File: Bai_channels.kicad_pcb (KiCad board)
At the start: 2 copper layers, 119 parts, among them Q1 BC337, Q10 BC337, Q11 BC337, Q12 BC337, Q2 BC337, Q3 BC337, Q4 BC337, Q5 BC337, Q6 BC337, Q7 BC337, Q8 BC337, Q9 BC337, U2 ATmega328-P, U3 LM7805_TO220

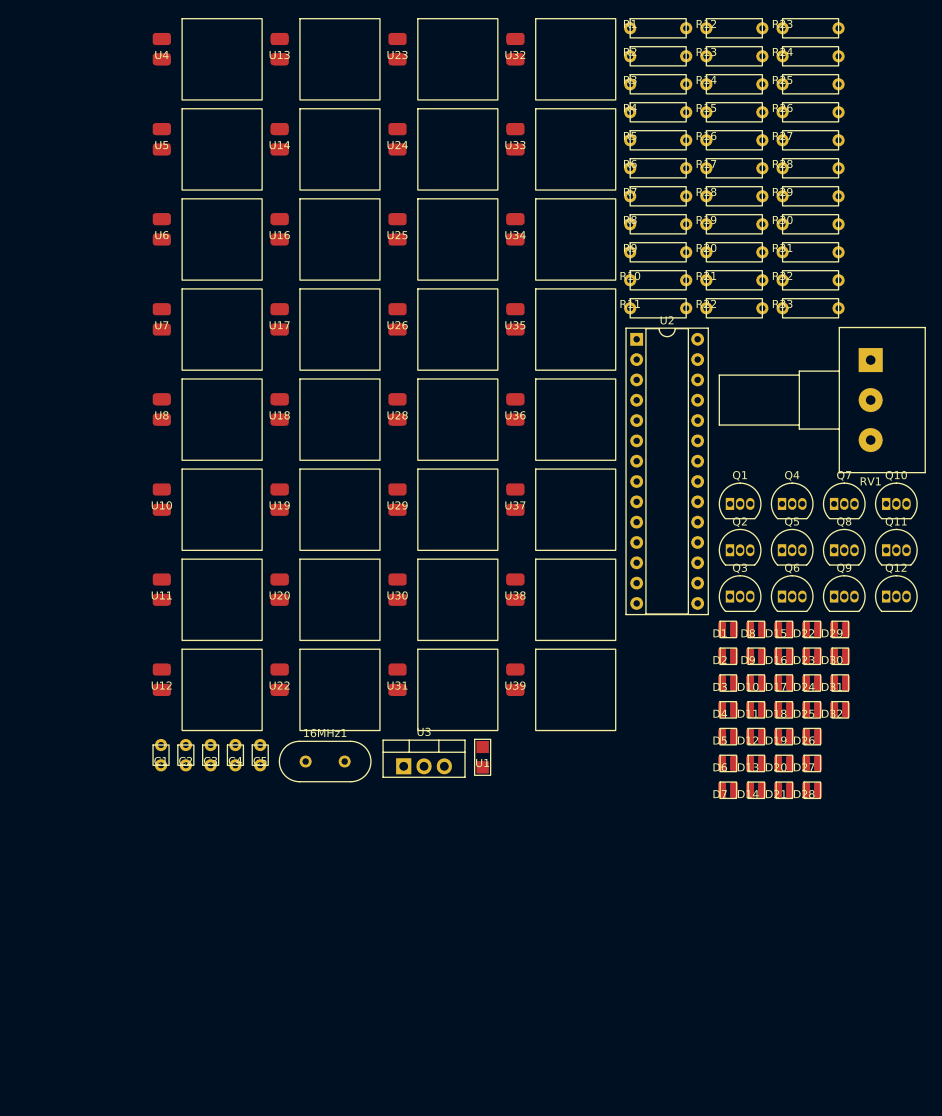
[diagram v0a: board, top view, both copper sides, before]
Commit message: custom cable footprint
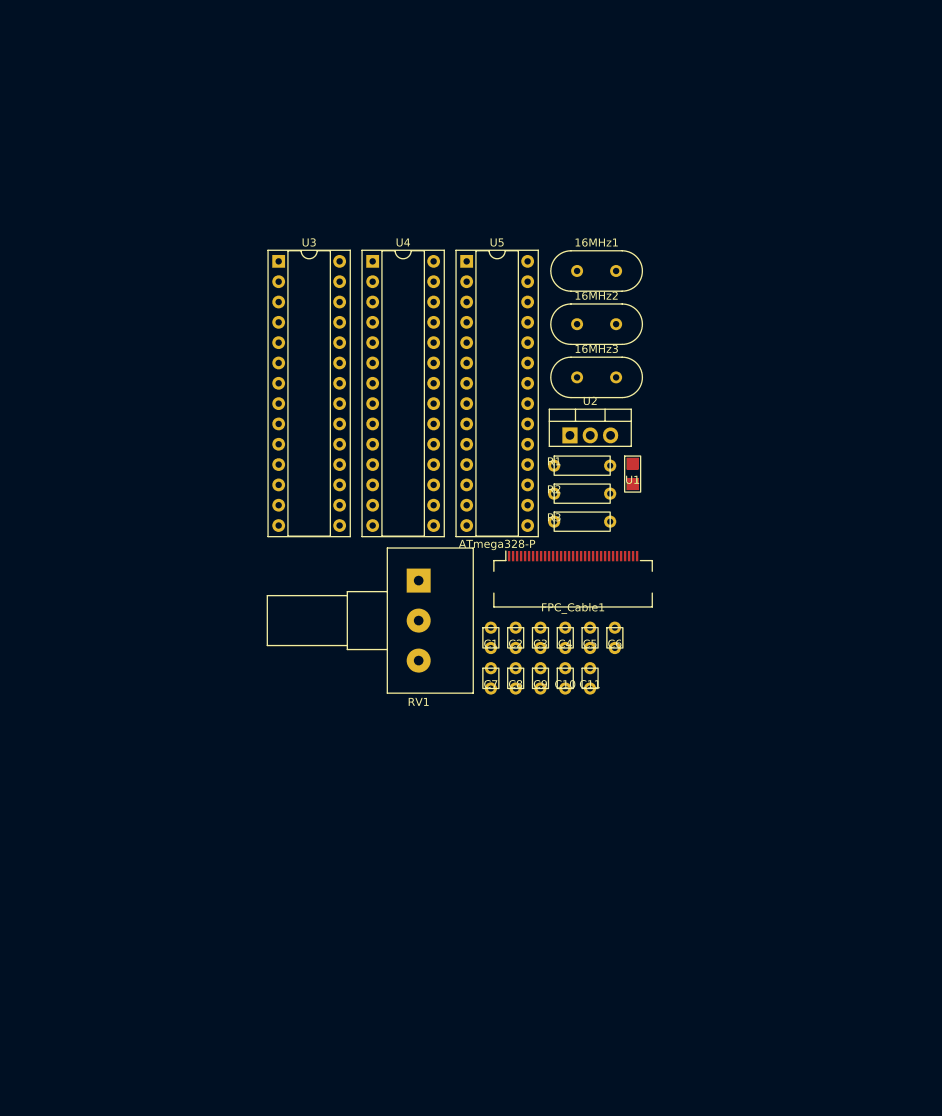
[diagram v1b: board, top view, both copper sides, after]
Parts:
- removed D1, D10, D11, D12, D13, D14, D15, D16, D17, D18, D19, D2, D20, D21, D22, D23, D24, D25, D26, D27, D28, D29, D3, D30, D31, D32, D4, D5, D6, D7, D8, D9: LED, custom:LED
- removed Q1, Q10, Q11, Q12, Q2, Q3, Q4, Q5, Q6, Q7, Q8, Q9: BC337, Package_TO_SOT_THT:TO-92_Inline
- removed R10, R11, R12, R13, R14, R15, R16, R17, R18, R19, R20, R21, R22, R23, R24, R25, R26, R27, R28, R29, R30, R31, R32, R33, R5, R6, R7, R8, R9: R, custom:R
- removed R4: 10kR, custom:R
- removed U10, U11, U12, U13, U14, U16, U17, U18, U19, U20, U22, U23, U24, U25, U26, U28, U29, U30, U31, U32, U33, U34, U35, U36, U37, U38, U39, U6, U7, U8: ~, custom:vibration_motor
- added 16MHz2: Crystal, Crystal:Crystal_HC49-4H_Vertical, F.Cu at (157.8, 81.4)
- added 16MHz3: Crystal, Crystal:Crystal_HC49-4H_Vertical, F.Cu at (157.8, 88.1)
- added C10: 22pF, custom:capacitor, F.Cu at (156.4, 127.0)
- added C11: 22pF, custom:capacitor, F.Cu at (159.5, 127.0)
- added C6: 22pF, custom:capacitor, F.Cu at (162.6, 121.9)
- added C7: 22pF, custom:capacitor, F.Cu at (147.1, 127.0)
- added C8: 22pF, custom:capacitor, F.Cu at (150.2, 127.0)
- added C9: 10µF, custom:capacitor, F.Cu at (153.3, 127.0)
- added FPC_Cable1: ~, custom:FPC_Cable, F.Cu at (157.3, 117.4)
- C2: value 22pF -> 1µF
- C3: value 22pF -> 10µF
- C4: value 1µF -> 10µF
- C5: value 10µF -> 22pF
- R1, R2, R3: value R -> 10kR
- U2: value ATmega328-P -> LM7805_TO220; footprint Package_DIP:DIP-28_W7.62mm_Socket -> Package_TO_SOT_THT:TO-220-3_Vertical
- U3: value LM7805_TO220 -> ATmega328-P; footprint Package_TO_SOT_THT:TO-220-3_Vertical -> Package_DIP:DIP-28_W7.62mm_Socket
- U4, U5: value ~ -> ATmega328-P; footprint custom:vibration_motor -> Package_DIP:DIP-28_W7.62mm_Socket
- moved 16MHz1 70.1 mm to (157.8, 74.8)
- moved U3 65.0 mm to (120.5, 73.6)
- moved RV1 62.9 mm to (138.0, 113.5)
- moved R1 55.5 mm to (155.0, 99.1)
- moved R2 55.5 mm to (155.0, 102.6)
- moved R3 55.5 mm to (155.0, 106.1)
- moved C4 43.8 mm to (156.4, 121.9)
- moved C1 43.8 mm to (147.1, 121.9)
- moved C5 43.8 mm to (159.5, 121.9)
- moved C2 43.8 mm to (150.2, 121.9)
- moved C3 43.8 mm to (153.3, 121.9)
- moved U5 40.6 mm to (144.0, 73.6)
- moved U1 40.1 mm to (164.8, 101.4)
- moved U4 36.5 mm to (132.3, 73.6)
- moved U2 14.6 mm to (156.9, 95.3)
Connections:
- 16MHz1 pad 1: Net-(U2-XTAL1/PB6) -> Net-(U3-XTAL1/PB6)
- 16MHz1 pad 2: Net-(U2-AVCC) -> Net-(U3-XTAL2/PB7)
- C1 pad 2: Net-(Q1-E) -> Net-(FPC_Cable1-GND)
- C2 pad 1: Net-(U2-AVCC) -> Net-(U2-VO)
- C2 pad 2: Net-(Q1-E) -> Net-(FPC_Cable1-GND)
- C3 pad 1: Net-(U2-XTAL1/PB6) -> Net-(U2-VO)
- C3 pad 2: Net-(Q1-E) -> Net-(FPC_Cable1-GND)
- C4 pad 1: Net-(U2-AVCC) -> Net-(U1-VCC)
- C4 pad 2: Net-(Q1-E) -> Net-(FPC_Cable1-GND)
- C5 pad 1: Net-(U2-AVCC) -> Net-(U3-XTAL2/PB7)
- C5 pad 2: Net-(Q1-E) -> Net-(FPC_Cable1-GND)
- R1 pad 1: Net-(D1-K) -> Net-(U3-~{RESET}/PC6)
- R1 pad 2: Net-(Q1-C) -> Net-(U2-VO)
- R2 pad 1: Net-(D2-K) -> Net-(U4-~{RESET}/PC6)
- R2 pad 2: Net-(Q2-C) -> Net-(U1-VCC)
- R3 pad 1: Net-(D3-K) -> Net-(U5-~{RESET}/PC6)
- R3 pad 2: Net-(Q3-C) -> Net-(U1-VCC)
- RV1 pad 1: Net-(Q1-E) -> Net-(FPC_Cable1-GND)
- RV1 pad 2: Net-(U2-PC0) -> Net-(U3-PC0)
- RV1 pad 3: Net-(U2-AVCC) -> Net-(U2-VO)
- U1 pad 2: Net-(Q1-E) -> Net-(FPC_Cable1-GND)
- U2 pad 1: Net-(U2-~{RESET}/PC6) -> Net-(U1-VCC)
- U2 pad 2: unconnected-(U2-PD0-Pad2) -> Net-(FPC_Cable1-GND)
- U2 pad 3: Net-(Q7-B) -> Net-(U2-VO)
- U3 pad 1: Net-(U1-VCC) -> Net-(U3-~{RESET}/PC6)
- U3 pad 2: Net-(Q1-E) -> Net-(U3-PD0)
- U3 pad 3: Net-(U2-AVCC) -> Net-(U3-PD1)
- U4 pad 1: Net-(D1-A) -> Net-(U4-~{RESET}/PC6)
- U4 pad 2: Net-(Q1-C) -> Net-(U4-PD0)
- U5 pad 1: Net-(D10-A) -> Net-(U5-~{RESET}/PC6)
- U5 pad 2: Net-(Q1-C) -> unconnected-(U5-PD0-Pad2)

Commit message: Official FPC
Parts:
- removed FPC_Cable1: ~, custom:FPC_Cable
- added J2: 5019514000, custom:CON_5019514000, F.Cu at (161.8, 115.8)
- moved C3 4.02 mm to (156.4, 124.5)
- moved C9 4.02 mm to (156.4, 129.5)
- moved C1 4.02 mm to (150.2, 124.5)
- moved C10 4.02 mm to (159.5, 129.5)
- moved C11 4.02 mm to (162.6, 129.5)
- moved C2 4.02 mm to (153.3, 124.5)
- moved C4 4.02 mm to (159.5, 124.5)
- moved C5 4.02 mm to (162.6, 124.5)
- moved C6 4.02 mm to (165.7, 124.5)
- moved C7 4.02 mm to (150.2, 129.5)
- moved C8 4.02 mm to (153.3, 129.5)
- moved U3 3.99 mm to (123.6, 76.1)
- moved 16MHz1 3.99 mm to (160.9, 77.3)
- moved 16MHz2 3.99 mm to (160.9, 83.9)
- moved 16MHz3 3.99 mm to (160.9, 90.6)
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
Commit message: traces
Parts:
- moved C11 54.4 mm to (113.0, 107.1), turned to -90 degrees
- moved C10 53.0 mm to (113.0, 104.0), turned to -90 degrees
- moved C9 51.9 mm to (113.0, 100.9), turned to -90 degrees
- moved 16MHz1 51.8 mm to (124.7, 114.3)
- moved C8 51.2 mm to (113.0, 97.8), turned to -90 degrees
- moved C7 50.9 mm to (113.0, 94.7), turned to -90 degrees
- moved C6 49.7 mm to (118.1, 110.2), turned to -90 degrees
- moved C5 47.7 mm to (118.1, 107.1), turned to -90 degrees
- moved R3 46.7 mm to (111.8, 114.3)
- moved C4 46.2 mm to (118.1, 104.0), turned to -90 degrees
- moved RV1 45.9 mm to (114.3, 78.7)
- moved C3 44.9 mm to (118.1, 100.9), turned to -90 degrees
- moved C2 44.1 mm to (118.1, 97.8), turned to -90 degrees
- moved C1 43.7 mm to (118.1, 94.7), turned to -90 degrees
- moved 16MHz2 38.4 mm to (137.4, 114.3)
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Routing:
- net Net-(U1-GND): track 0.00 -> 154.2 mm, vias 0 -> 4
- net Net-(U1-VCC): track 0.00 -> 118.3 mm
- net Net-(U2-VO): track 0.00 -> 110.4 mm, vias 0 -> 2
- net Net-(U3-PD4): track 0.00 -> 103.9 mm, vias 0 -> 5
- net Net-(U3-~{RESET}/PC6): track 0.00 -> 103.2 mm, vias 0 -> 3
- net Net-(U4-~{RESET}/PC6): track 0.00 -> 89.7 mm, vias 0 -> 2
- net Net-(U3-PD2): track 0.00 -> 86.4 mm, vias 0 -> 2
- net Net-(U3-PB4): track 0.00 -> 76.8 mm, vias 0 -> 6
- net Net-(U3-PD0): track 0.00 -> 74.1 mm, vias 0 -> 1
- net Net-(U5-~{RESET}/PC6): track 0.00 -> 73.6 mm
- net Net-(U5-XTAL1/PB6): track 0.00 -> 59.9 mm, vias 0 -> 3
- net Net-(U5-XTAL2/PB7): track 0.00 -> 57.4 mm, vias 0 -> 1
- net Net-(U4-PD7): track 0.00 -> 55.7 mm, vias 0 -> 7
- net Net-(U3-PB2): track 0.00 -> 55.6 mm, vias 0 -> 4
- net Net-(U3-PB0): track 0.00 -> 55.2 mm, vias 0 -> 3
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
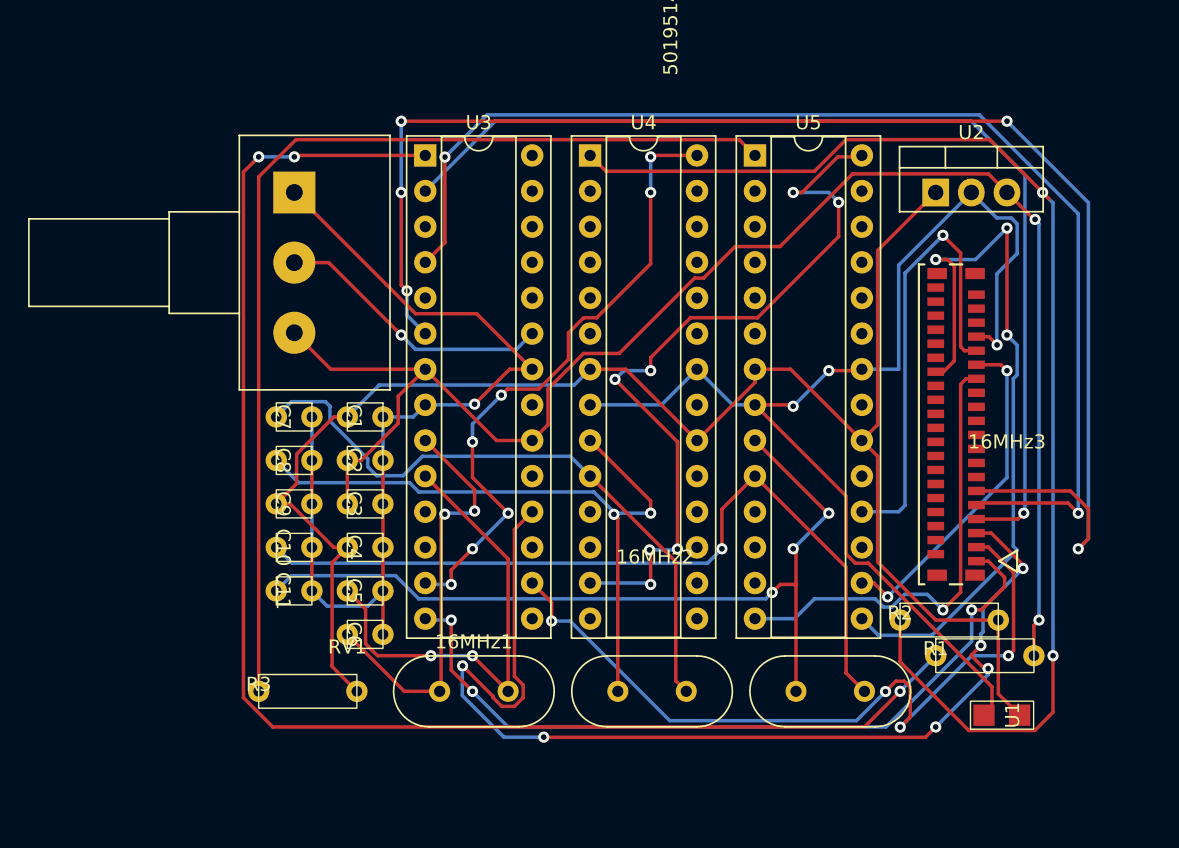
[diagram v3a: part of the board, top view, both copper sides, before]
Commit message: two-layer routing complete pray for 3-layer possibility
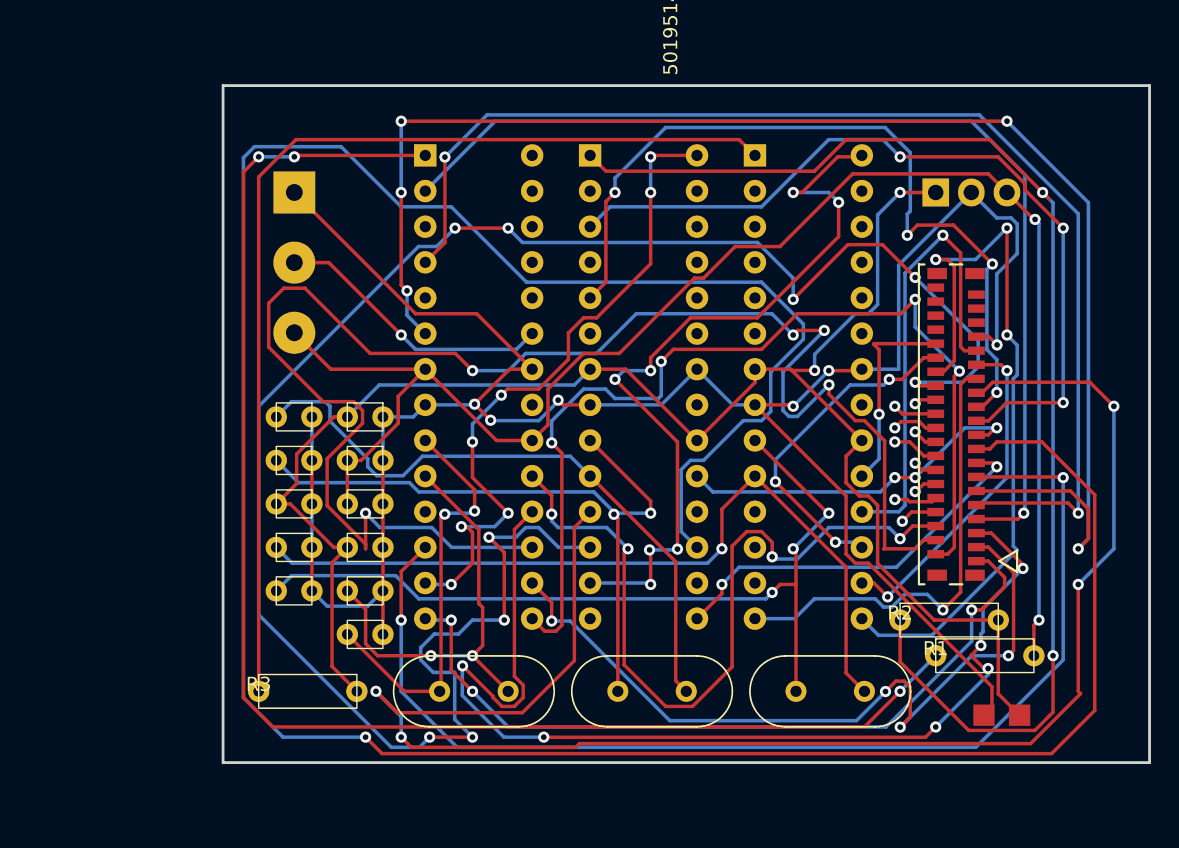
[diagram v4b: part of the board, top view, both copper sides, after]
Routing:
- net Net-(U4-PB3): track 0.00 -> 194.4 mm, vias 0 -> 1
- net Net-(U4-PD6): track 0.00 -> 136.7 mm, vias 0 -> 9
- net Net-(U4-PD5): track 0.00 -> 114.1 mm, vias 0 -> 4
- net Net-(U3-PB3): track 0.00 -> 113.1 mm, vias 0 -> 5
- net Net-(U3-PD6): track 0.00 -> 81.6 mm, vias 0 -> 2
- net Net-(U3-PB1): track 0.00 -> 69.7 mm, vias 0 -> 4
- net Net-(U4-PD1): track 0.00 -> 58.3 mm, vias 0 -> 3
- net Net-(U4-PD3): track 0.00 -> 57.5 mm, vias 0 -> 4
- net Net-(U3-PB5): track 0.00 -> 55.1 mm, vias 0 -> 4
- net Net-(U4-PB1): track 0.00 -> 27.8 mm, vias 0 -> 2
- net Net-(U4-PB5): track 0.00 -> 25.4 mm, vias 0 -> 3
- net Net-(U5-PB3): track 0.00 -> 24.2 mm, vias 0 -> 3
- net Net-(U5-PB5): track 0.00 -> 14.5 mm, vias 0 -> 1
- net Net-(U1-GND): track 154.2 -> 163.8 mm, vias 4 -> 6
- net Net-(U4-PB2): track 0.00 -> 3.33 mm, vias 0 -> 1
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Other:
- board outline added: 66 x 48.3 mm

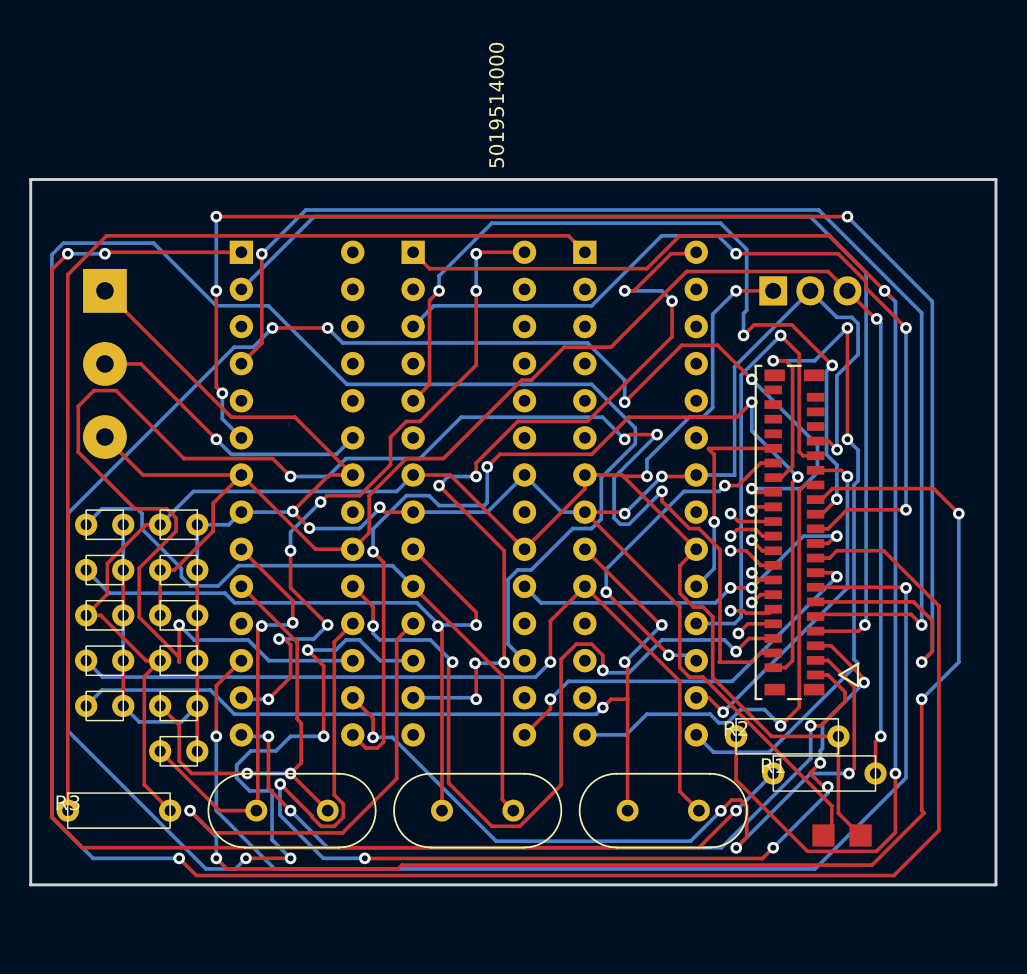
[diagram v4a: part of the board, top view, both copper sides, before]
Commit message: board complete with four layers
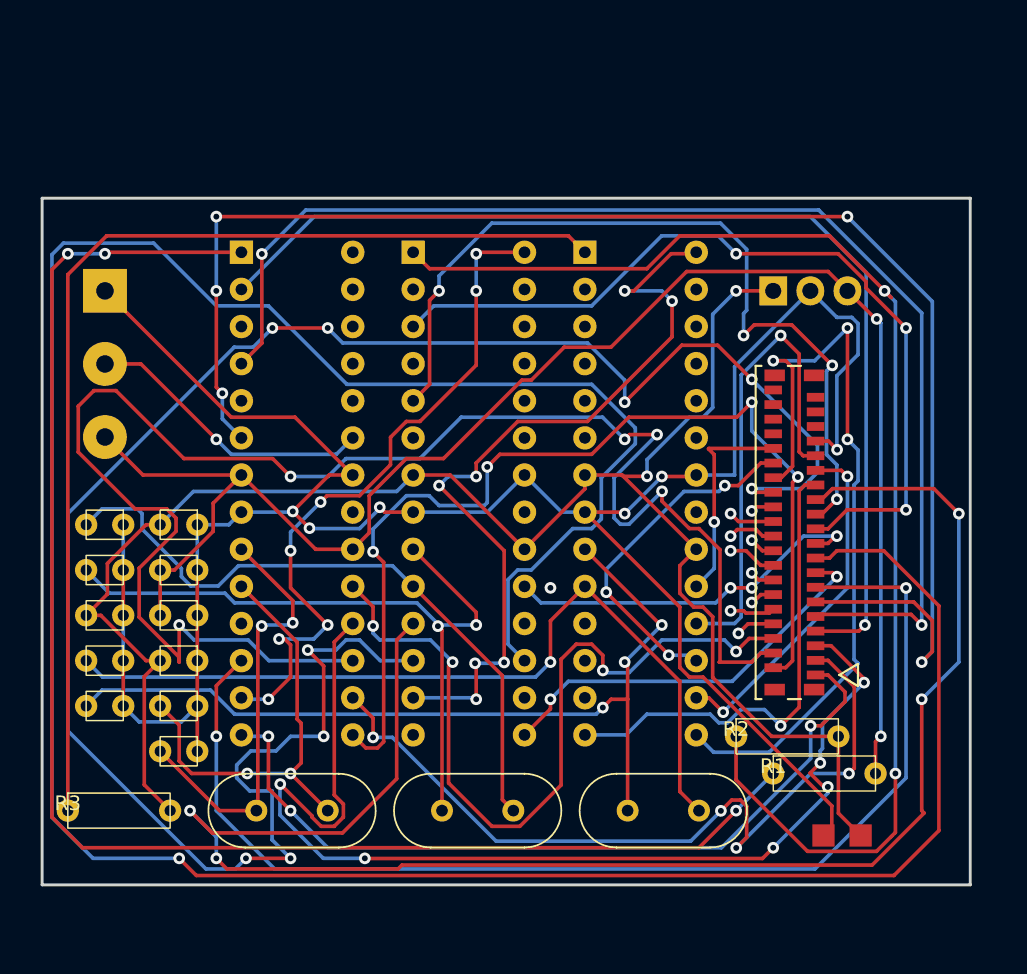
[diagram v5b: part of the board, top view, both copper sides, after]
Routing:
- net Net-(U3-PD1): track 2.65 -> 73.1 mm
- net Net-(U3-PD5): track 1.69 -> 68.6 mm
- net Net-(U3-PD3): track 3.09 -> 66.2 mm
- net Net-(U4-PD0): track 3.29 -> 39.4 mm
- net Net-(U4-PD2): track 3.14 -> 36.8 mm
- net Net-(U4-PB0): track 1.67 -> 30.6 mm
- net Net-(U4-PD4): track 1.58 -> 28.7 mm
- net Net-(U4-PB2): track 3.33 -> 25.8 mm, vias 1 -> 2
- net Net-(U4-PB4): track 1.77 -> 20.2 mm
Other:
- board size 66 x 48.3 mm -> 63.5 x 47 mm
- copper layers 2 -> 4
